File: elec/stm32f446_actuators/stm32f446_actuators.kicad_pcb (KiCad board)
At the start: 2 copper layers, 88 x 70 mm, 172 parts, among them IC1 TS2596CM550_RNG, J1 Conn_01x02, J11 1, J13 2, J15 3, J17 0, J18 4, J19 4, J2 USB_B_Micro, J21 0, J22 3, J23 1, J24 5, J25 5, J27 1, J28 4, J29 +VBAT, J3 USART, J30 2, J31 6, J32 2, J33 5, J34 +5V, J35 GND, J36 3, J37 7, J38 Conn_01x04, J39 Conn_01x04, J4 SWD, J40 0, J41 2, J42 4, J43 Conn_01x04, J44 Conn_01x04, J45 1, J46 3, J5 0, J6 Conn_01x04, J7 Conn_01x04, J8 1, J9 0, Q1 IRLZ44N, Q11 IRLZ44N, Q3 IRLZ44N, Q5 IRLZ44N, Q7 IRLZ44N, Q9 IRLZ44N, SW1 RESET, U1 MIC5504-3.3YM5, U2 STM32F103CBTx, U3 MIC5504-3.3YM5, U4 STM32F446RETx, Y1 8MHz(12pF), Y2 8MHz(16pF)[N/A]

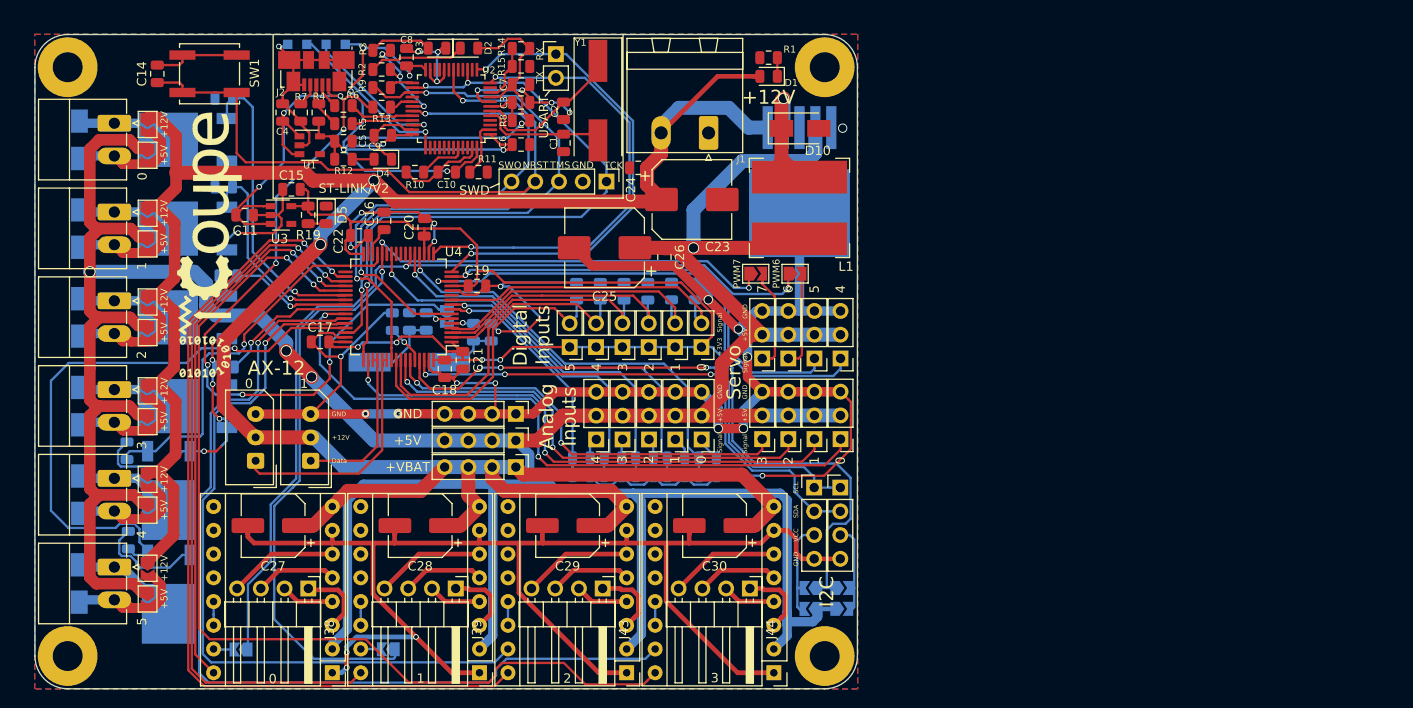
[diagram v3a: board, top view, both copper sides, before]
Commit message: Fix missing vias
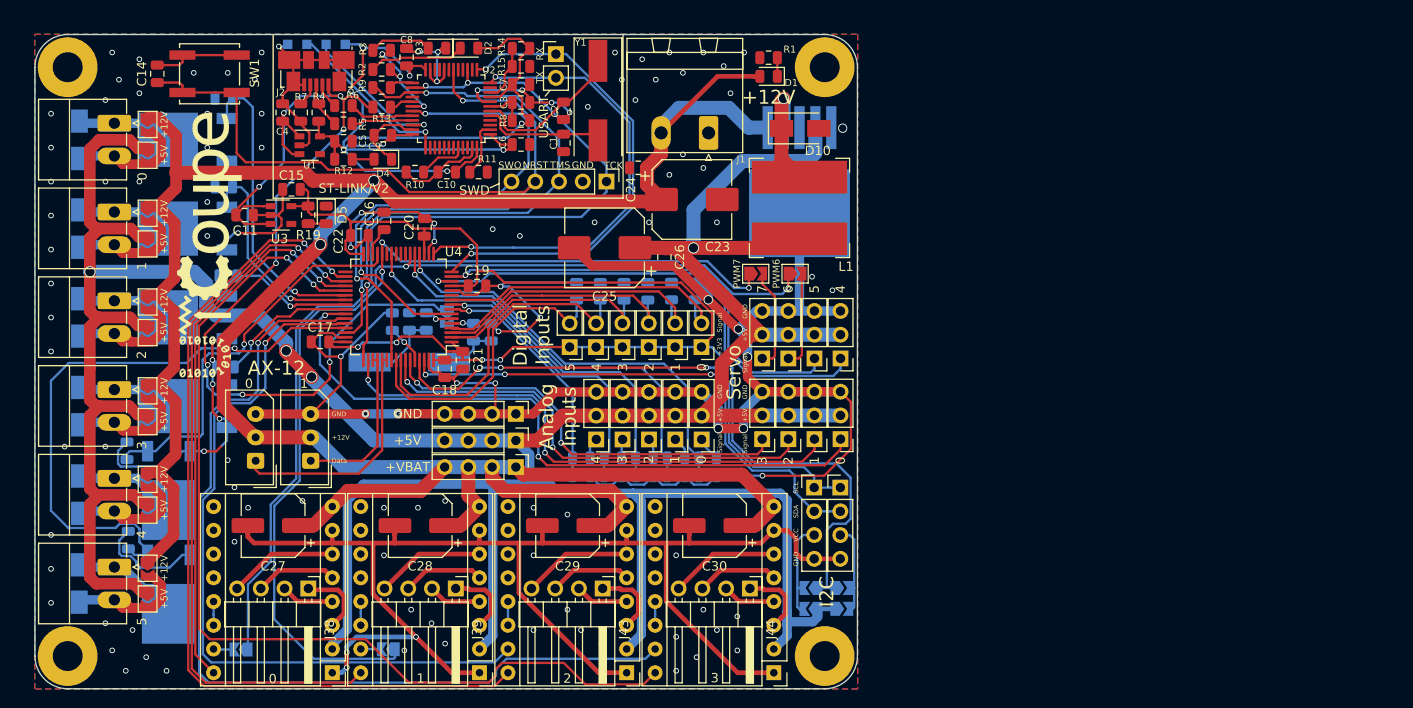
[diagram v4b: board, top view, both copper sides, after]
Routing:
- net GND: vias 35 -> 123
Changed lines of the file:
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@@
     (thickness 1.6)
     (drawings 55)
-    (tracks 1770)
+    (tracks 1859)
     (zones 0)
     (modules 172)
@@
   (segment (start 134.433592 97.20901) (end 137.296801 94.345801) (width 0.25) (layer F.Cu) (net 3))
   (segment (start 127.8382 97.20901) (end 134.433592 97.20901) (width 0.25) (layer F.Cu) (net 3))
+  (via (at 51.722668 58.4655) (size 0.6) (drill 0.4) (layers F.Cu B.Cu) (net 3))
+  (via (at 51.722668 62.1005) (size 0.6) (drill 0.4) (layers F.Cu B.Cu) (net 3))
+  (via (at 51.722668 65.7355) (size 0.6) (drill 0.4) (layers F.Cu B.Cu) (net 3))
+  (via (at 51.722668 69.3705) (size 0.6) (drill 0.4) (layers F.Cu B.Cu) (net 3))
+  (via (at 51.722668 73.0055) (size 0.6) (drill 0.4) (layers F.Cu B.Cu) (net 3))
+  (via (at 51.722668 76.6405) (size 0.6) (drill 0.4) (layers F.Cu B.Cu) (net 3))
+  (via (at 51.722668 80.2755) (size 0.6) (drill 0.4) (layers F.Cu B.Cu) (net 3))
+  (via (at 51.722668 83.9105) (size 0.6) (drill 0.4) (layers F.Cu B.Cu) (net 3))
+  (via (at 51.722668 103.5395) (size 0.6) (drill 0.4) (layers F.Cu B.Cu) (net 3))
+  (via (at 51.722668 107.1745) (size 0.6) (drill 0.4) (layers F.Cu B.Cu) (net 3))
+  (via (at 51.722668 110.8095) (size 0.6) (drill 0.4) (layers F.Cu B.Cu) (net 3))
+  (via (at 53.176668 94.0885) (size 0.6) (drill 0.4) (layers F.Cu B.Cu) (net 3))
+  (via (at 57.538668 57.0115) (size 0.6) (drill 0.4) (layers F.Cu B.Cu) (net 3))
+  (via (at 57.538668 65.7355) (size 0.6) (drill 0.4) (layers F.Cu B.Cu) (net 3))
+  (via (at 57.538668 94.0885) (size 0.6) (drill 0.4) (layers F.Cu B.Cu) (net 3))
+  (via (at 57.538668 112.9905) (size 0.6) (drill 0.4) (layers F.Cu B.Cu) (net 3))
+  (via (at 58.265668 51.9225) (size 0.6) (drill 0.4) (layers F.Cu B.Cu) (net 3))
+  (via (at 58.265668 115.8985) (size 0.6) (drill 0.4) (layers F.Cu B.Cu) (net 3))
+  (via (at 58.992668 54.8305) (size 0.6) (drill 0.4) (layers F.Cu B.Cu) (net 3))
+  (via (at 59.719668 118.0795) (size 0.6) (drill 0.4) (layers F.Cu B.Cu) (net 3))
+  (via (at 60.446668 113.7175) (size 0.6) (drill 0.4) (layers F.Cu B.Cu) (net 3))
+  (via (at 61.173668 52.6495) (size 0.6) (drill 0.4) (layers F.Cu B.Cu) (net 3))
+  (via (at 61.173668 56.2845) (size 0.6) (drill 0.4) (layers F.Cu B.Cu) (net 3))
+  (via (at 61.173668 65.7355) (size 0.6) (drill 0.4) (layers F.Cu B.Cu) (net 3))
+  (via (at 61.900668 116.6255) (size 0.6) (drill 0.4) (layers F.Cu B.Cu) (net 3))
+  (via (at 64.081668 118.0795) (size 0.6) (drill 0.4) (layers F.Cu B.Cu) (net 3))
+  (via (at 66.989668 54.1035) (size 0.6) (drill 0.4) (layers F.Cu B.Cu) (net 3))
+  (via (at 68.443668 58.4655) (size 0.6) (drill 0.4) (layers F.Cu B.Cu) (net 3))
+  (via (at 68.443668 62.1005) (size 0.6) (drill 0.4) (layers F.Cu B.Cu) (net 3))
+  (via (at 68.443668 67.9165) (size 0.6) (drill 0.4) (layers F.Cu B.Cu) (net 3))
+  (via (at 68.443668 71.5515) (size 0.6) (drill 0.4) (layers F.Cu B.Cu) (net 3))
+  (via (at 70.624668 54.1035) (size 0.6) (drill 0.4) (layers F.Cu B.Cu) (net 3))
+  (via (at 70.624668 95.5425) (size 0.6) (drill 0.4) (layers F.Cu B.Cu) (net 3))
+  (via (at 71.351668 98.4505) (size 0.6) (drill 0.4) (layers F.Cu B.Cu) (net 3))
+  (via (at 71.351668 104.2665) (size 0.6) (drill 0.4) (layers F.Cu B.Cu) (net 3))
+  (via (at 72.805668 100.6315) (size 0.6) (drill 0.4) (layers F.Cu B.Cu) (net 3))
+  (via (at 73.532668 54.8305) (size 0.6) (drill 0.4) (layers F.Cu B.Cu) (net 3))
+  (via (at 74.259668 51.9225) (size 0.6) (drill 0.4) (layers F.Cu B.Cu) (net 3))
+  (via (at 74.259668 58.4655) (size 0.6) (drill 0.4) (layers F.Cu B.Cu) (net 3))
+  (via (at 74.259668 62.1005) (size 0.6) (drill 0.4) (layers F.Cu B.Cu) (net 3))
+  (via (at 78.621668 99.9045) (size 0.6) (drill 0.4) (layers F.Cu B.Cu) (net 3))
+  (via (at 87.345668 100.6315) (size 0.6) (drill 0.4) (layers F.Cu B.Cu) (net 3))
+  (via (at 87.345668 105.7205) (size 0.6) (drill 0.4) (layers F.Cu B.Cu) (net 3))
+  (via (at 89.526668 115.8985) (size 0.6) (drill 0.4) (layers F.Cu B.Cu) (net 3))
+  (via (at 90.253668 111.5365) (size 0.6) (drill 0.4) (layers F.Cu B.Cu) (net 3))
+  (via (at 90.980668 100.6315) (size 0.6) (drill 0.4) (layers F.Cu B.Cu) (net 3))
+  (via (at 92.434668 112.9905) (size 0.6) (drill 0.4) (layers F.Cu B.Cu) (net 3))
+  (via (at 93.888668 99.9045) (size 0.6) (drill 0.4) (layers F.Cu B.Cu) (net 3))
+  (via (at 93.888668 115.1715) (size 0.6) (drill 0.4) (layers F.Cu B.Cu) (net 3))
+  (via (at 95.342668 59.9195) (size 0.6) (drill 0.4) (layers F.Cu B.Cu) (net 3))
+  (via (at 98.977668 70.8245) (size 0.6) (drill 0.4) (layers F.Cu B.Cu) (net 3))
+  (via (at 101.885668 71.5515) (size 0.6) (drill 0.4) (layers F.Cu B.Cu) (net 3))
+  (via (at 103.339668 100.6315) (size 0.6) (drill 0.4) (layers F.Cu B.Cu) (net 3))
+  (via (at 103.339668 105.7205) (size 0.6) (drill 0.4) (layers F.Cu B.Cu) (net 3))
+  (via (at 103.339668 113.7175) (size 0.6) (drill 0.4) (layers F.Cu B.Cu) (net 3))
+  (via (at 106.974668 101.3585) (size 0.6) (drill 0.4) (layers F.Cu B.Cu) (net 3))
+  (via (at 106.974668 111.5365) (size 0.6) (drill 0.4) (layers F.Cu B.Cu) (net 3))
+  (via (at 108.428668 113.7175) (size 0.6) (drill 0.4) (layers F.Cu B.Cu) (net 3))
+  (via (at 109.155668 57.7385) (size 0.6) (drill 0.4) (layers F.Cu B.Cu) (net 3))
+  (via (at 109.882668 70.0975) (size 0.6) (drill 0.4) (layers F.Cu B.Cu) (net 3))
+  (via (at 110.609668 115.1715) (size 0.6) (drill 0.4) (layers F.Cu B.Cu) (net 3))
+  (via (at 112.063668 51.9225) (size 0.6) (drill 0.4) (layers F.Cu B.Cu) (net 3))
+  (via (at 112.790668 54.8305) (size 0.6) (drill 0.4) (layers F.Cu B.Cu) (net 3))
+  (via (at 114.244668 57.0115) (size 0.6) (drill 0.4) (layers F.Cu B.Cu) (net 3))
+  (via (at 114.971668 52.6495) (size 0.6) (drill 0.4) (layers F.Cu B.Cu) (net 3))
+  (via (at 115.698668 70.0975) (size 0.6) (drill 0.4) (layers F.Cu B.Cu) (net 3))
+  (via (at 116.425668 54.8305) (size 0.6) (drill 0.4) (layers F.Cu B.Cu) (net 3))
+  (via (at 117.879668 51.9225) (size 0.6) (drill 0.4) (layers F.Cu B.Cu) (net 3))
+  (via (at 117.879668 65.0085) (size 0.6) (drill 0.4) (layers F.Cu B.Cu) (net 3))
+  (via (at 118.606668 105.7205) (size 0.6) (drill 0.4) (layers F.Cu B.Cu) (net 3))
+  (via (at 118.606668 114.4445) (size 0.6) (drill 0.4) (layers F.Cu B.Cu) (net 3))
+  (via (at 118.606668 118.0795) (size 0.6) (drill 0.4) (layers F.Cu B.Cu) (net 3))
+  (via (at 119.333668 54.1035) (size 0.6) (drill 0.4) (layers F.Cu B.Cu) (net 3))
+  (via (at 119.333668 62.8275) (size 0.6) (drill 0.4) (layers F.Cu B.Cu) (net 3))
+  (via (at 120.787668 116.6255) (size 0.6) (drill 0.4) (layers F.Cu B.Cu) (net 3))
+  (via (at 121.514668 51.9225) (size 0.6) (drill 0.4) (layers F.Cu B.Cu) (net 3))
+  (via (at 121.514668 64.2815) (size 0.6) (drill 0.4) (layers F.Cu B.Cu) (net 3))
+  (via (at 121.514668 111.5365) (size 0.6) (drill 0.4) (layers F.Cu B.Cu) (net 3))
+  (via (at 122.968668 70.0975) (size 0.6) (drill 0.4) (layers F.Cu B.Cu) (net 3))
+  (via (at 122.968668 113.7175) (size 0.6) (drill 0.4) (layers F.Cu B.Cu) (net 3))
+  (via (at 123.695668 53.3765) (size 0.6) (drill 0.4) (layers F.Cu B.Cu) (net 3))
+  (via (at 124.422668 56.2845) (size 0.6) (drill 0.4) (layers F.Cu B.Cu) (net 3))
+  (via (at 125.149668 112.2635) (size 0.6) (drill 0.4) (layers F.Cu B.Cu) (net 3))
+  (via (at 125.149668 115.8985) (size 0.6) (drill 0.4) (layers F.Cu B.Cu) (net 3))
+  (via (at 125.876668 51.9225) (size 0.6) (drill 0.4) (layers F.Cu B.Cu) (net 3))
+  (via (at 133.146668 75.9135) (size 0.6) (drill 0.4) (layers F.Cu B.Cu) (net 3))
+  (via (at 135.327668 77.3675) (size 0.6) (drill 0.4) (layers F.Cu B.Cu) (net 3))
+  (segment (start 104.066668 80.2755) (end 104.066668 80.2755) (width 0.25) (layer F.Cu) (net 3))
+  (via (at 104.066668 80.2755) (size 0.6) (drill 0.4) (layers F.Cu B.Cu) (net 3))
   (via (at 97.86 84.81) (size 0.6) (drill 0.4) (layers F.Cu B.Cu) (net 4))
   (segment (start 85.15 73.4714) (end 85.15 74.208864) (width 0.25) (layer F.Cu) (net 4))

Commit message: Fix missing via
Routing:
- net GND: track 540.8 -> 540.9 mm, vias 123 -> 124
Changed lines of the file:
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@@
     (thickness 1.6)
     (drawings 55)
-    (tracks 1859)
+    (tracks 1861)
     (zones 0)
     (modules 172)
@@
     (tags "DPAK TO-252 DPAK-3 TO-252-3 SOT-428")
     (attr smd)
-    (fp_text reference Q11 (at 0 4.5 90) (layer B.SilkS)
+    (fp_text reference Q11 (at 3.7084 4.7117 90) (layer B.SilkS)
       (effects (font (size 1 1) (thickness 0.15)) (justify mirror))
     )
@@
     (tags "DPAK TO-252 DPAK-3 TO-252-3 SOT-428")
     (attr smd)
-    (fp_text reference Q9 (at 0 4.5 90) (layer B.SilkS)
+    (fp_text reference Q9 (at -2.1971 -4.3434 90) (layer B.SilkS)
       (effects (font (size 1 1) (thickness 0.15)) (justify mirror))
     )
@@
   (segment (start 69.441611 90.809801) (end 69.74161 91.1098) (width 0.25) (layer F.Cu) (net 3))
   (segment (start 69.017798 90.385988) (end 69.441611 90.809801) (width 0.25) (layer F.Cu) (net 3))
-  (segment (start 70.5448 93.441368) (end 69.897668 94.0885) (width 0.25) (layer B.Cu) (net 3))
-  (segment (start 70.5448 92.0436) (end 70.5448 93.441368) (width 0.25) (layer B.Cu) (net 3))
   (segment (start 70.165874 91.1098) (end 69.74161 91.1098) (width 0.25) (layer B.Cu) (net 3))
   (segment (start 70.2564 91.1098) (end 70.165874 91.1098) (width 0.25) (layer B.Cu) (net 3))
@@
   (segment (start 70.5448 91.3982) (end 70.2564 91.1098) (width 0.25) (layer B.Cu) (net 3))
   (via (at 68.0974 94.5896) (size 0.6) (drill 0.4) (layers F.Cu B.Cu) (net 3))
-  (segment (start 69.897668 94.0885) (end 69.396568 94.5896) (width 0.25) (layer F.Cu) (net 3))
-  (segment (start 69.396568 94.5896) (end 68.521664 94.5896) (width 0.25) (layer F.Cu) (net 3))
-  (segment (start 68.521664 94.5896) (end 68.0974 94.5896) (width 0.25) (layer F.Cu) (net 3))
+  (segment (start 69.897668 94.0885) (end 69.877284 94.108884) (width 0.25) (layer F.Cu) (net 3))
   (segment (start 66.6182 94.5806) (end 68.0884 94.5806) (width 0.25) (layer B.Cu) (net 3))
   (segment (start 68.0884 94.5806) (end 68.0974 94.5896) (width 0.25) (layer B.Cu) (net 3))
@@
   (segment (start 104.066668 80.2755) (end 104.066668 80.2755) (width 0.25) (layer F.Cu) (net 3))
   (via (at 104.066668 80.2755) (size 0.6) (drill 0.4) (layers F.Cu B.Cu) (net 3))
+  (via (at 69.877284 94.108884) (size 0.6) (drill 0.4) (layers F.Cu B.Cu) (net 3))
+  (segment (start 70.5448 93.441368) (end 69.877284 94.108884) (width 0.25) (layer B.Cu) (net 3))
+  (segment (start 70.5448 92.0436) (end 70.5448 93.441368) (width 0.25) (layer B.Cu) (net 3))
+  (segment (start 68.521664 94.5896) (end 68.0974 94.5896) (width 0.25) (layer F.Cu) (net 3))
+  (segment (start 69.877284 94.108884) (end 69.396568 94.5896) (width 0.25) (layer F.Cu) (net 3))
+  (segment (start 69.396568 94.5896) (end 68.521664 94.5896) (width 0.25) (layer F.Cu) (net 3))
   (via (at 97.86 84.81) (size 0.6) (drill 0.4) (layers F.Cu B.Cu) (net 4))
   (segment (start 85.15 73.4714) (end 85.15 74.208864) (width 0.25) (layer F.Cu) (net 4))

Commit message: Fix serial 3 and 5 reversed labels
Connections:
- J5 pad 1: /Actuators/RX3 -> /Actuators/RX5
- J8 pad 1: /Actuators/RX5 -> /Actuators/RX3
- U4 pad 51: /Actuators/RX5 -> /Actuators/RX3
- U4 pad 52: /Actuators/RX5 -> /Actuators/RX3
- U4 pad 53: /Actuators/RX3 -> /Actuators/RX5
- U4 pad 54: /Actuators/RX3 -> /Actuators/RX5
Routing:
- net /Actuators/RX5: track 17.5 -> 25.9 mm
- net /Actuators/RX3: track 25.9 -> 17.5 mm
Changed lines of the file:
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@@
       (net 24 /STM32F446RE6/SWO))
     (pad 54 smd roundrect (at 1.25 -5.675 180) (size 0.3 1.55) (layers F.Cu F.Paste F.Mask) (roundrect_rratio 0.25)
-      (net 103 /Actuators/RX3))
+      (net 104 /Actuators/RX5))
     (pad 53 smd roundrect (at 1.75 -5.675 180) (size 0.3 1.55) (layers F.Cu F.Paste F.Mask) (roundrect_rratio 0.25)
-      (net 103 /Actuators/RX3))
-    (pad 52 smd roundrect (at 2.25 -5.675 180) (size 0.3 1.55) (layers F.Cu F.Paste F.Mask) (roundrect_rratio 0.25)
       (net 104 /Actuators/RX5))
+    (pad 52 smd roundrect (at 2.25 -5.675 180) (size 0.3 1.55) (layers F.Cu F.Paste F.Mask) (roundrect_rratio 0.25)
+      (net 103 /Actuators/RX3))
     (pad 51 smd roundrect (at 2.75 -5.675 180) (size 0.3 1.55) (layers F.Cu F.Paste F.Mask) (roundrect_rratio 0.25)
-      (net 104 /Actuators/RX5))
+      (net 103 /Actuators/RX3))
     (pad 50 smd roundrect (at 3.25 -5.675 180) (size 0.3 1.55) (layers F.Cu F.Paste F.Mask) (roundrect_rratio 0.25)
       (net 109 /Actuators/PWM1))
@@
     )
     (pad 1 thru_hole roundrect (at 0 0 90) (size 1.7 1.85) (drill 0.85) (layers *.Cu *.Mask) (roundrect_rratio 0.147059)
-      (net 104 /Actuators/RX5))
+      (net 103 /Actuators/RX3))
     (pad 2 thru_hole oval (at 2.5 0 90) (size 1.7 1.85) (drill 0.85) (layers *.Cu *.Mask)
       (net 2 +12V))
@@
     )
     (pad 1 thru_hole roundrect (at 0 0 90) (size 1.7 1.85) (drill 0.85) (layers *.Cu *.Mask) (roundrect_rratio 0.147059)
-      (net 103 /Actuators/RX3))
+      (net 104 /Actuators/RX5))
     (pad 2 thru_hole oval (at 2.5 0 90) (size 1.7 1.85) (drill 0.85) (layers *.Cu *.Mask)
       (net 2 +12V))
@@
   (segment (start 59.3962 110.4848) (end 60.27481 111.36341) (width 1) (layer F.Cu) (net 102))
   (segment (start 63.50221 108.873444) (end 62.653865 108.025099) (width 1) (layer F.Cu) (net 102))
-  (segment (start 73.6092 96.5556) (end 74.0336 96.98) (width 0.25) (layer F.Cu) (net 103))
-  (segment (start 73.6092 95.6056) (end 73.6092 96.5556) (width 0.25) (layer F.Cu) (net 103))
-  (segment (start 74.0336 96.98) (end 84.64 96.98) (width 0.25) (layer F.Cu) (net 103))
-  (segment (start 87.15 94.47) (end 87.15 84.8214) (width 0.25) (layer F.Cu) (net 103))
-  (segment (start 84.64 96.98) (end 87.15 94.47) (width 0.25) (layer F.Cu) (net 103))
-  (segment (start 87.15 84.8214) (end 87.65 84.8214) (width 0.25) (layer F.Cu) (net 103))
-  (segment (start 86.65 94.01) (end 86.65 84.8214) (width 0.25) (layer F.Cu) (net 104))
-  (segment (start 79.502 95.6056) (end 85.0544 95.6056) (width 0.25) (layer F.Cu) (net 104))
-  (segment (start 85.0544 95.6056) (end 86.65 94.01) (width 0.25) (layer F.Cu) (net 104))
-  (segment (start 86.65 84.8214) (end 86.15 84.8214) (width 0.25) (layer F.Cu) (net 104))
+  (segment (start 73.6092 96.5556) (end 74.0336 96.98) (width 0.25) (layer F.Cu) (net 104))
+  (segment (start 73.6092 95.6056) (end 73.6092 96.5556) (width 0.25) (layer F.Cu) (net 104))
+  (segment (start 74.0336 96.98) (end 84.64 96.98) (width 0.25) (layer F.Cu) (net 104))
+  (segment (start 87.15 94.47) (end 87.15 84.8214) (width 0.25) (layer F.Cu) (net 104))
+  (segment (start 84.64 96.98) (end 87.15 94.47) (width 0.25) (layer F.Cu) (net 104))
+  (segment (start 87.15 84.8214) (end 87.65 84.8214) (width 0.25) (layer F.Cu) (net 104))
+  (segment (start 86.65 94.01) (end 86.65 84.8214) (width 0.25) (layer F.Cu) (net 103))
+  (segment (start 79.502 95.6056) (end 85.0544 95.6056) (width 0.25) (layer F.Cu) (net 103))
+  (segment (start 85.0544 95.6056) (end 86.65 94.01) (width 0.25) (layer F.Cu) (net 103))
+  (segment (start 86.65 84.8214) (end 86.15 84.8214) (width 0.25) (layer F.Cu) (net 103))
   (via (at 81.042262 80.041569) (size 0.6) (drill 0.4) (layers F.Cu B.Cu) (net 105))
   (segment (start 81.187431 79.8964) (end 83.225 79.8964) (width 0.25) (layer F.Cu) (net 105))
